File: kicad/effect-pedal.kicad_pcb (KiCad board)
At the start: 2 copper layers, 85 parts, among them J1 NJ3FD-V, J10 USB_C_Receptacle_USB2.0_14P, J11 Conn_ST_STDC14, J12 Barrel_Jack, J2 NJ3FD-V, J3 Conn_01x08, J4 Conn_01x06, J5 Conn_01x06, J6 SOIC Bite Connector, J7 SOIC Bite Connector, J8 SOIC Bite Connector, J9 SOIC Bite Connector, Q1 NMOS, Q2 NMOS, SW1 RotaryEncoder_Switch, SW2 RotaryEncoder_Switch, SW3 RotaryEncoder_Switch, SW4 RotaryEncoder_Switch, SW6 SW_SPDT, SW7 SW_Push, U1 STM32H723ZGTx, U2 PCM5102A, U3 USBLC6-2SC6, U4 TPS62142, Y1 Crystal

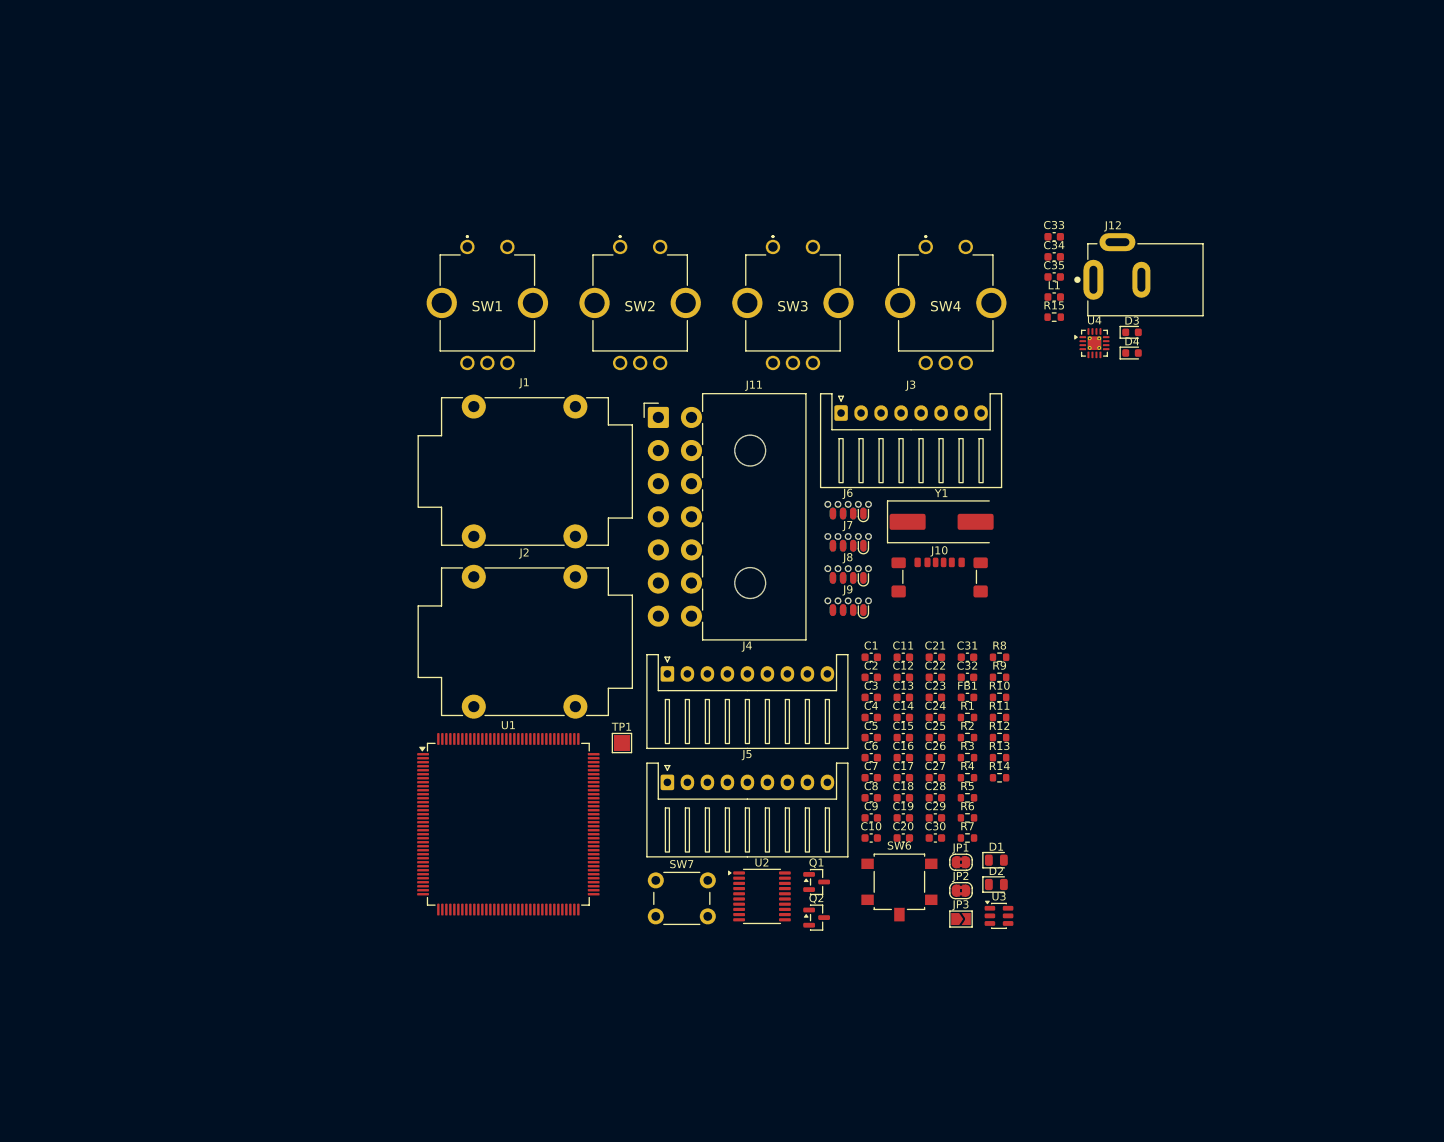
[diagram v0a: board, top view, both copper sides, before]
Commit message: Finish part sourcing and start PCB layout
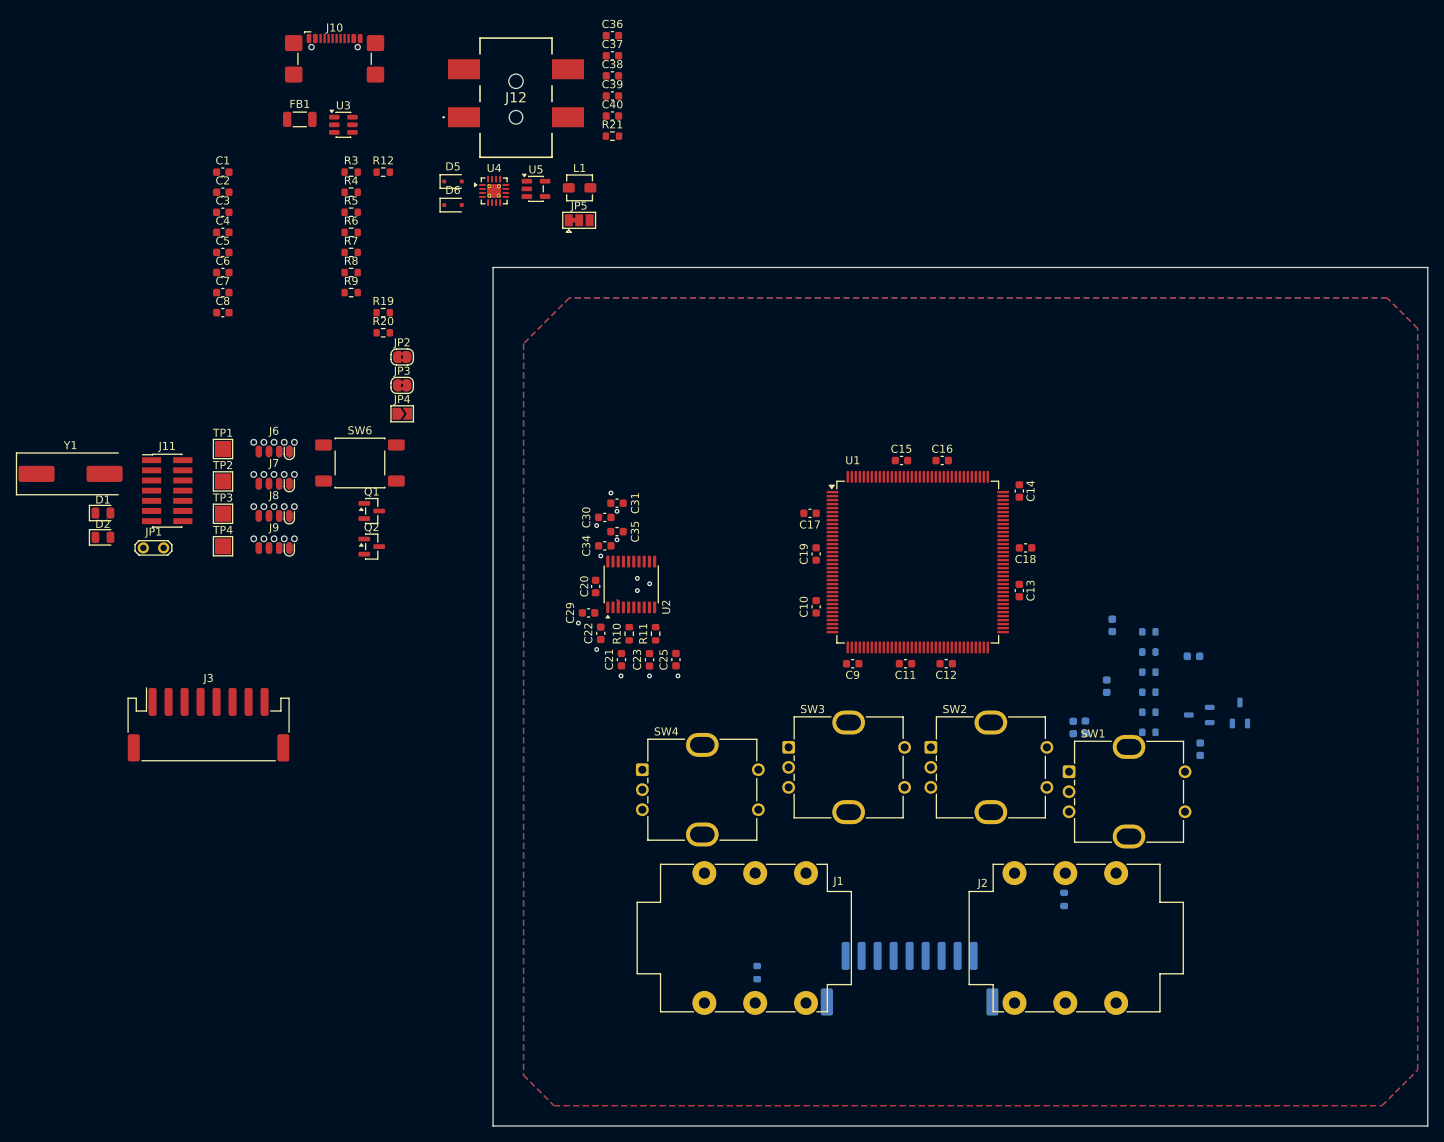
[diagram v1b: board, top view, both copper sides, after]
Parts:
- removed J4: Conn_01x06, Connector_JST:JST_XH_S9B-XH-A_1x09_P2.50mm_Horizontal
- removed SW7: SW_Push, Button_Switch_THT:SW_PUSH_6mm
- added C36: 10u, Capacitor_SMD:C_0603_1608Metric, F.Cu at (105.1, 9.13)
- added C37: 390p, Capacitor_SMD:C_0603_1608Metric, F.Cu at (105.1, 11.6)
- added C38: 22u, Capacitor_SMD:C_0603_1608Metric, F.Cu at (105.1, 14.2)
- added C39: 4.7u, Capacitor_SMD:C_0603_1608Metric, F.Cu at (105.1, 16.7)
- added C40: 1u, Capacitor_SMD:C_0603_1608Metric, F.Cu at (105.1, 19.2)
- added D5: D_Schottky, Diode_SMD:D_SOD-323F, F.Cu at (85.2, 27.4)
- added D6: D_Schottky, Diode_SMD:D_SOD-323F, F.Cu at (85.2, 30.3)
- added JP4: SolderJumper_2_Open, Jumper:SolderJumper-2_P1.3mm_Open_TrianglePad1.0x1.5mm, F.Cu at (78.8, 56.4)
- added JP5: SolderJumper_3_Bridged12, Jumper:SolderJumper-3_P1.3mm_Bridged12_Pad1.0x1.5mm, F.Cu at (100.9, 32.2)
- added R16: 100k, Resistor_SMD:R_0603_1608Metric, B.Cu at (172.1, 91.2)
- added R17: 100, Resistor_SMD:R_0603_1608Metric, B.Cu at (172.1, 93.7)
- added R18: 100, Resistor_SMD:R_0603_1608Metric, B.Cu at (172.1, 96.2)
- added R19: 5.1k, Resistor_SMD:R_0603_1608Metric, F.Cu at (76.4, 43.8)
- added R20: 5.1k, Resistor_SMD:R_0603_1608Metric, F.Cu at (76.4, 46.3)
- added R21: 100k, Resistor_SMD:R_0603_1608Metric, F.Cu at (105.1, 21.7)
- added TP2: TestPoint, TestPoint:TestPoint_Pad_2.0x2.0mm, F.Cu at (56.4, 64.8)
- added TP3: TestPoint, TestPoint:TestPoint_Pad_2.0x2.0mm, F.Cu at (56.4, 68.9)
- added TP4: TestPoint, TestPoint:TestPoint_Pad_2.0x2.0mm, F.Cu at (56.4, 72.9)
- added U5: LP5907MFX-3.0, Package_TO_SOT_SMD:SOT-23-5, F.Cu at (95.5, 28.3)
- C10, C11, C12, C13, C14, C15, C16, C17, C18, C7, C9: value 100n -> 0.1u
- C19: value 10u -> 0.1u
- C20: value 0.1u -> 2.2u
- C23: value 2.2u -> 2.2n
- C24: value 10u -> 0.1u; moved to B.Cu
- C26: value 10n -> 10u; moved to B.Cu
- C27: value 2.2n -> 10u; moved to B.Cu
- C28, R15: moved to B.Cu
- C30: value 15u -> 10u
- C31: value .1u -> 10u
- C32: value .1u -> 10n; moved to B.Cu
- C33: value 10u -> 10n; moved to B.Cu
- C34: value 390p -> 0.1u
- C35: value 22u -> 0.1u
- C8: value 100n -> 1u
- D3, D4: value D -> D_Schottky_Dual_Series_ACK_Split; footprint Diode_SMD:D_0603_1608Metric -> Package_TO_SOT_SMD:TSOT-23; moved to B.Cu
- FB1: footprint Inductor_SMD:L_0603_1608Metric -> Inductor_SMD:L_1206_3216Metric
- J1, J2: value NJ3FD-V -> NJ6FD-H; footprint Connector_Audio:Jack_6.35mm_Neutrik_NMJ4HCD2_Horizontal -> Connector_Audio:Jack_6.35mm_Neutrik_NMJ6HCD3_Horizontal
- J10: footprint Connector_USB:USB_C_Receptacle_GCT_USB4135-GF-A_6P_TopMnt_Horizontal -> Connector_USB:USB_C_Receptacle_GCT_USB4110
- J11: footprint Connector_TE-Connectivity:TE_MATE-N-LOK_1-770973-x_2x07_P4.14mm_Horizontal -> Connector_PinHeader_1.27mm:PinHeader_2x07_P1.27mm_Vertical_SMD
- J12: footprint SameSky:CUI_PJ-002A -> SameSky:PJ002AHSMTTR
- J3: footprint Connector_JST:JST_XH_S8B-XH-A_1x08_P2.50mm_Horizontal -> Connector_JST:JST_PH_S8B-PH-SM4-TB_1x08-1MP_P2.00mm_Horizontal
- J5: value Conn_01x06 -> Conn_01x09; footprint Connector_JST:JST_XH_S9B-XH-A_1x09_P2.50mm_Horizontal -> Connector_JST:JST_PH_S9B-PH-SM4-TB_1x09-1MP_P2.00mm_Horizontal; moved to B.Cu
- JP1: value SolderJumper_2_Bridged -> Jumper_2_Open; footprint Jumper:SolderJumper-2_P1.3mm_Bridged2Bar_RoundedPad1.0x1.5mm -> TestPoint:TestPoint_2Pads_Pitch2.54mm_Drill0.8mm
- JP3: value SolderJumper_2_Open -> SolderJumper_2_Bridged; footprint Jumper:SolderJumper-2_P1.3mm_Open_TrianglePad1.0x1.5mm -> Jumper:SolderJumper-2_P1.3mm_Bridged2Bar_RoundedPad1.0x1.5mm
- L1: footprint Inductor_SMD:L_0603_1608Metric -> Inductor_SMD:L_Vishay_IHLP-1212
- R1: value 100k -> 1M; moved to B.Cu
- R11: value 3.3k -> 470
- R12: value 3.3k -> 100k
- R13, R14: value 5.1k -> 100k; moved to B.Cu
- R2: value 3.3k -> 1M; moved to B.Cu
- R3, R6: value 10k -> 100k
- R4: value 100k -> 3.3k
- R5: value 3.3k -> 10k
- R7: value 10k -> 3.3k
- R8: value 100k -> 10k
- R9: value 470 -> 10k
- SW1, SW2, SW3, SW4: footprint Bournes:PEC11L4115FS0020 -> Bournes:RotaryEncoder_Bourns_Vertical_PEC12R-3x17F-Sxxxx
- SW6: value SW_SPDT -> SW_Push; footprint Button_Switch_SMD:SW_SPST_B3S-1100 -> Button_Switch_SMD:SW_Push_1P1T_NO_E-Switch_TL3301NxxxxxG
- moved U3 128.4 mm to (71.5, 20.3)
- moved D1 119.8 mm to (41.4, 68.8)
- moved D2 119.8 mm to (41.4, 71.8)
- moved FB1 110.4 mm to (66.0, 19.6)
- moved JP1 109.5 mm to (46.5, 73.2)
- moved Y1 109.0 mm to (37.4, 63.9)
- moved R3 106.3 mm to (72.4, 26.2)
- moved R4 106.3 mm to (72.4, 28.7)
- moved R5 106.3 mm to (72.4, 31.2)
- moved R6 106.3 mm to (72.4, 33.7)
- moved R7 106.3 mm to (72.4, 36.2)
- moved R12 104.6 mm to (76.4, 26.2)
- moved C1 101.2 mm to (56.4, 26.2)
- moved C2 101.2 mm to (56.4, 28.7)
- moved C3 101.2 mm to (56.4, 31.2)
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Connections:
- C20 pad 1: VCC -> Net-(U2-CAPM)
- C20 pad 2: GND -> Net-(U2-CAPP)
- C22 pad 1: VCC -> VDDA
- C23 pad 1: Net-(U2-CAPM) -> GND
- C23 pad 2: Net-(U2-CAPP) -> /AUD_WET_L
- C24 pad 1: VCC -> VDDA
- C25 pad 2: /AUD_WET_L -> /AUD_WET_R
- C26 pad 1: GND -> VDDA
- C26 pad 2: Net-(C26-Pad2) -> GND
- C27 pad 1: GND -> /AUD_IN_L
- C27 pad 2: /AUD_WET_R -> Net-(C27-Pad2)
- C28 pad 1: Net-(U2-LDOO) -> /AUD_IN_R
- C28 pad 2: GND -> Net-(C28-Pad2)
- C30 pad 1: Net-(C26-Pad2) -> VCC
- C30 pad 2: /AUD_IN_GND -> GND
- C32 pad 2: VDDA -> /AUD_IN_L_BIAS
- C33 pad 1: /Power/VIN -> GND
- C33 pad 2: GND -> /AUD_IN_R_BIAS
- C34 pad 1: Net-(U4-SS/TR) -> VCC
- C35 pad 1: VCC -> GND
- C35 pad 2: GND -> Net-(U2-LDOO)
- C8 pad 1: VCC -> GND
- C8 pad 2: GND -> /VREF+
- D3 pad 1: /Power/VIN -> GND
- D3 pad 2: USB_VBUS -> /VREF+
- D4 pad 1: /Power/VIN -> GND
- D4 pad 2: Net-(D4-A) -> /VREF+
- J1 pad S: /AUD_IN_GND -> GND
- J1 pad SN: (no net) -> /AUD_N
- J1 pad TN: (no net) -> /AUD_N
- J10 pad S1: /SHIELD -> GNDPWR
- J12 pad 2: Net-(D4-A) -> Net-(D6-A)
- J12 pad 3: (no net) -> GNDPWR
- J2 pad SN: (no net) -> /AUD_N
- J2 pad TN: (no net) -> /AUD_N
- J3 pad 1: VCC -> /DISPLAY_BL
- J3 pad 2: GND -> /DISPLAY_RST
- J3 pad 3: /DISPLAY_DATA -> /DISPLAY_DC
- J3 pad 4: /DISPLAY_SCK -> /DISPLAY_CS
- J3 pad 5: /DISPLAY_CS -> /DISPLAY_SCK
- J3 pad 6: /DISPLAY_DC -> /DISPLAY_DATA
- J3 pad 7: /DISPLAY_RST -> GND
- J3 pad 8: /DISPLAY_BL -> VCC
- J5 pad 3: /AUD_IN_GND -> GND
- J6 pad 1: /AUD_IN_R_AMP -> /AUD_IN_R_BIAS
- J6 pad 3: /AUD_IN_L_AMP -> /AUD_IN_L_BIAS
- J6 pad 7: /AUD_IN_GND -> /AUD_IN_R_AMP
- JP1 pad 1: /DEBUG_RST -> VCC
- JP1 pad 2: /RESET -> /BOOT
- JP2 pad 1: VCC -> /DEBUG_RST
- JP2 pad 2: Net-(JP2-B) -> /RESET
- JP3 pad 2: /VREF+ -> Net-(JP3-B)
- R1 pad 1: /LED_1 -> /AUD_N
- R10 pad 1: Net-(U2-OUTR) -> /AUD_WET_L
- R10 pad 2: /AUD_WET_R -> Net-(U2-OUTL)
- R11 pad 1: /VREF+ -> /AUD_WET_R
- R11 pad 2: Net-(C26-Pad2) -> Net-(U2-OUTR)
- R12 pad 1: Net-(C26-Pad2) -> GNDPWR
- R13 pad 1: /CC2 -> /VREF+
- R13 pad 2: GND -> Net-(C27-Pad2)
- R14 pad 1: /CC1 -> Net-(C27-Pad2)
- R15 pad 1: VCC -> /VREF+
- R15 pad 2: Net-(U4-PG) -> Net-(C28-Pad2)
- R2 pad 1: VCC -> /AUD_N
- R2 pad 2: Net-(Q1-D) -> GND
- R3 pad 1: /BOOT -> /LED_1
- R3 pad 2: Net-(SW6-B) -> GND
- R4 pad 1: /LED_2 -> VCC
- R4 pad 2: GND -> Net-(Q1-D)
- R5 pad 1: VCC -> /BOOT
- R5 pad 2: Net-(Q2-D) -> GND
- R6 pad 1: VCC -> /LED_2
- R6 pad 2: /RESET -> GND
- R7 pad 1: /UNUSED -> VCC
- R7 pad 2: GND -> Net-(Q2-D)
- R8 pad 1: GND -> VCC
- R8 pad 2: /SHIELD -> /RESET
- R9 pad 1: /AUD_WET_L -> /UNUSED
- R9 pad 2: Net-(U2-OUTL) -> GND
- SW6 pad 2: Net-(SW6-B) -> /RESET
- TP1 pad 1: Net-(U1-VBAT) -> VCC
- U1 pad 46: /AUD_IN_R -> /AUD_IN_R_BIAS
- U1 pad 6: Net-(U1-VBAT) -> VCC
- U1 pad 60: /AUD_IN_L -> /AUD_IN_L_BIAS
- U1 pad 95: Net-(JP2-B) -> Net-(JP3-B)
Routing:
- net GND: track 0.00 -> 0.93 mm, vias 0 -> 11
- net VCC: vias 0 -> 2
- added copper zone on B.Cu, net GND
- added copper zone on F.Cu, net GND
- added copper zone on In1.Cu, net GND
- added copper zone on In2.Cu, net VCC
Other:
- board outline added: 116.8 x 107.3 mm
- copper layers 2 -> 4

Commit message: Finish schematic
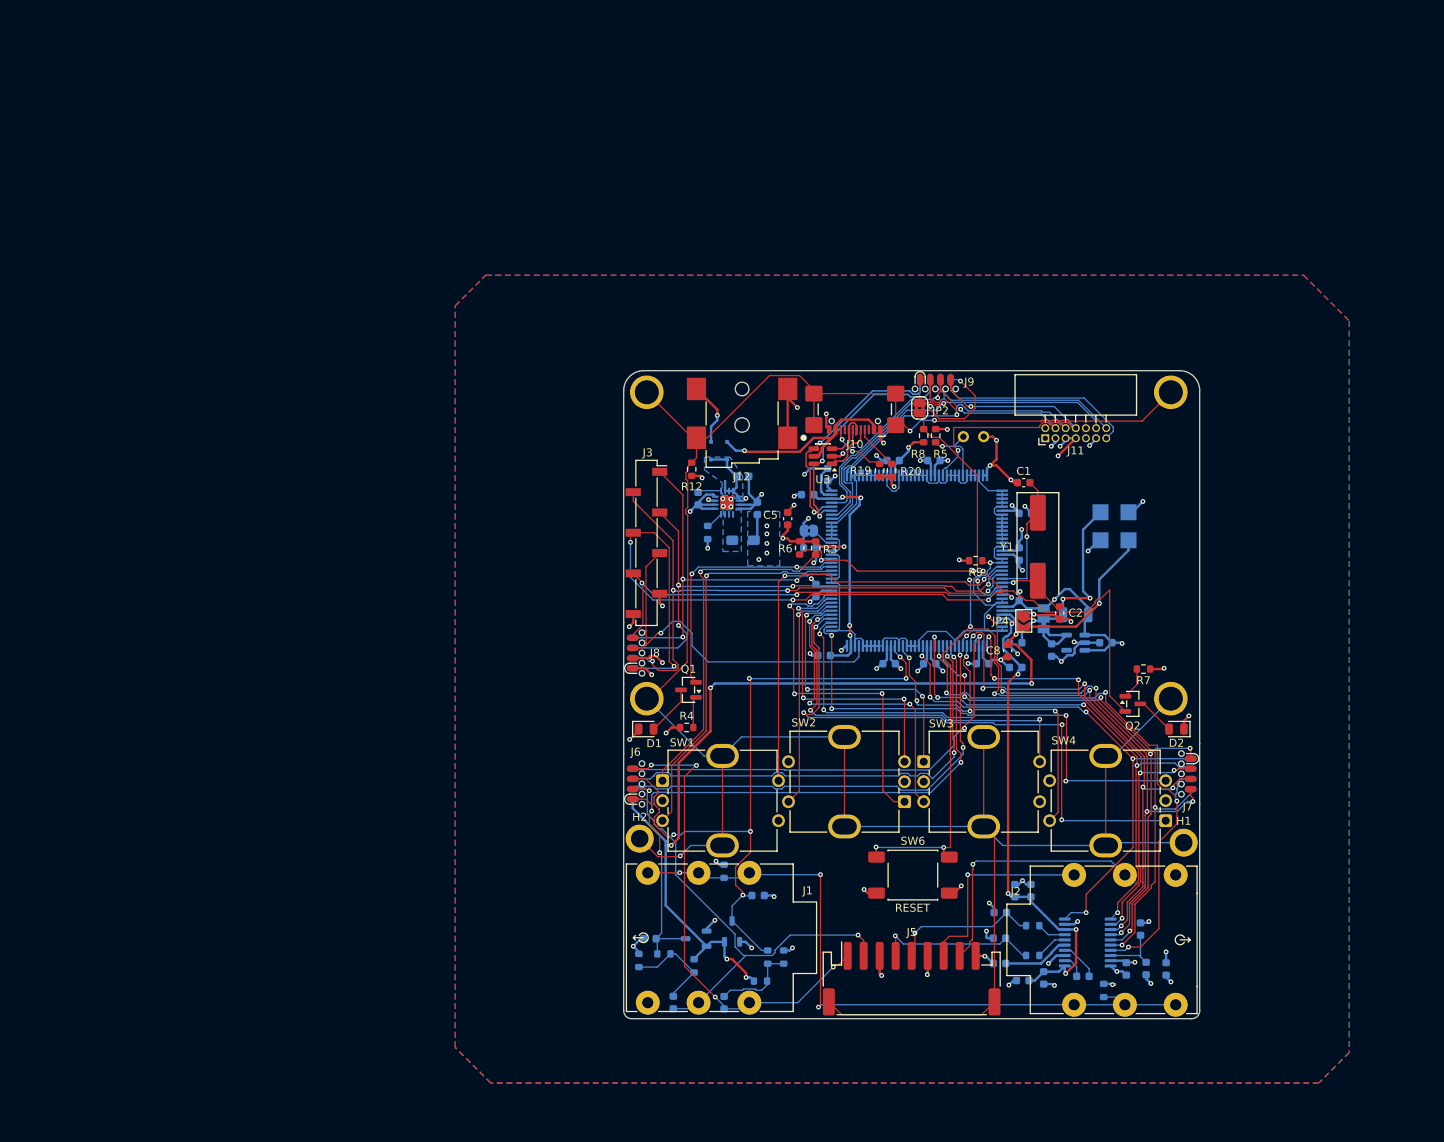
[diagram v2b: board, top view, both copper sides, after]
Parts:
- added H1: MountingHole_Pad, MountingHole:MountingHole_2.2mm_M2_ISO7380_Pad, F.Cu at (176.5, 110.0)
- added H2: MountingHole_Pad, MountingHole:MountingHole_2.2mm_M2_ISO7380_Pad, F.Cu at (108.5, 109.5)
- C10, C11, C12, C13, C14, C15, C16, C17, C18, C19, C20, C21, C22, C23, C25, C29, C3, C30, C31, C34, C35, C36, C37, C38, C39, C4, C40, C6, C7, C9, D5, D6, FB1, JP1, JP3, JP5, L1, R10, R11, R21, TP1, TP2, TP3, TP4, U1, U2, U4, U5: moved to B.Cu
- J1, J2: value NJ6FD-H -> NMJ6HCD3; footprint Connector_Audio:Jack_6.35mm_Neutrik_NMJ6HCD3_Horizontal -> Neutrik:Jack_6.35mm_Neutrik_NMJ6HCD3_Horizontal
- J10: footprint Connector_USB:USB_C_Receptacle_GCT_USB4110 -> Custom:USB_C_Receptacle_GCT_USB4110
- J11: footprint Connector_PinHeader_1.27mm:PinHeader_2x07_P1.27mm_Vertical_SMD -> Custom:STDC14_Connector
- J12: footprint SameSky:PJ002AHSMTTR -> Custom:CUI_PJ-002AH-SMT-TR
- J3: footprint Connector_JST:JST_PH_S8B-PH-SM4-TB_1x08-1MP_P2.00mm_Horizontal -> Waveshare:Waveshare_2.4in_LCD
- J5: footprint Connector_JST:JST_PH_S9B-PH-SM4-TB_1x09-1MP_P2.00mm_Horizontal -> Custom:JST_PH_S9B-PH-SM4-TB_1x09-1MP_P2.00mm_Horizontal; moved to F.Cu
- moved D2 136.3 mm to (175.6, 95.8), turned to 180 degrees
- moved Y1 121.3 mm to (158.3, 73.0), turned to -90 degrees
- moved J7 120.7 mm to (178.1, 101.4), turned to 90 degrees
- moved C2 117.1 mm to (161.0, 81.3), turned to -90 degrees
- moved FB1 115.1 mm to (163.0, 81.5), turned to 180 degrees
- moved TP1 113.5 mm to (169.6, 68.7), turned to 180 degrees
- moved TP3 113.2 mm to (169.6, 72.2), turned to 180 degrees
- moved R7 111.9 mm to (171.5, 88.3), turned to 180 degrees
- moved C6 110.7 mm to (155.5, 88.1), turned to 180 degrees
- moved J11 110.0 mm to (159.2, 59.5), turned to 90 degrees
- moved TP2 109.8 mm to (166.1, 68.7), turned to 180 degrees
- moved TP4 109.7 mm to (166.1, 72.2), turned to 180 degrees
- moved C7 108.3 mm to (155.5, 85.0), turned to 180 degrees
- moved C1 107.4 mm to (156.5, 65.0)
- moved C8 106.8 mm to (154.5, 86.0), turned to 90 degrees
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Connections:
- net Net-(D6-A) renamed /Power/VIN_JACK
- net Net-(JP5-A) renamed /Power/PWR_LDO_OUT
- net Net-(L1-Pad1) renamed /Power/PWR_SW
- net Net-(U4-PG) renamed /Power/PG
- net Net-(U4-SS/TR) renamed /Power/SS
- JP4 pad 1: VCC -> VDDA
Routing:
- net GNDPWR: track 0.00 -> 301.2 mm, vias 0 -> 3
- net GND: track 0.93 -> 173.2 mm, vias 11 -> 64
- net /VREF+: track 0.00 -> 130.2 mm, vias 0 -> 7
- net /UNUSED: track 0.00 -> 126.0 mm, vias 0 -> 1
- net VCC: track 0.00 -> 97.5 mm, vias 2 -> 34
- net VDDA: track 0.00 -> 87.4 mm, vias 0 -> 8
- net /AUD_IN_L_BIAS: track 0.00 -> 85.8 mm, vias 0 -> 6
- net /AUD_IN_R_BIAS: track 0.00 -> 83.4 mm, vias 0 -> 4
- net /AUD_N: track 0.00 -> 83.2 mm, vias 0 -> 3
- net /DISPLAY_CS: track 0.00 -> 78.9 mm, vias 0 -> 4
- net /RESET: track 0.00 -> 77.9 mm, vias 0 -> 5
- net /DISPLAY_RST: track 0.00 -> 74.2 mm, vias 0 -> 4
- net /EDAC_XSMT: track 0.00 -> 73.9 mm, vias 0 -> 5
- net /ENC4_L: track 0.00 -> 73.1 mm, vias 0 -> 4
- net /DISPLAY_BL: track 0.00 -> 70.1 mm, vias 0 -> 4
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- added copper zone on B.Cu, net /Power/PWR_SW
- added copper zone on B.Cu, net /Power/VIN
- added copper zone on B.Cu, net VCC
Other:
- board size 116.8 x 107.3 mm -> 72 x 81 mm
- board text added: "Digital Effect Pedal v1 Edith Boles Ethan Ferguson Muhammad-Abdullah Abdelqader Nick Nikander Shaelin Olton"
- board text added: "GND"
- board text added: "RESET"
- board text added: "VCC"
- board text added: "VDDA"
- board text added: "VREF+"

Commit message: Setup for production
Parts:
- U4: footprint Package_DFN_QFN:VQFN-16-1EP_3x3mm_P0.5mm_EP1.68x1.68mm_ThermalVias -> Custom:VQFN-16-1EP_3x3mm_P0.5mm_EP1.68x1.68mm_ThermalVias
- moved TP1 5.20 mm to (169.6, 63.5)
- moved TP2 5.20 mm to (166.1, 63.5)
- moved TP3 5.20 mm to (169.6, 67.0)
- moved TP4 5.20 mm to (166.1, 67.0)
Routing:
- net VDDA: track 87.4 -> 93.3 mm
- net /VREF+: track 130.2 -> 135.3 mm
- net /LED_1: track 35.0 -> 38.3 mm
- net /ENC1_B: track 31.8 -> 34.7 mm
- net GNDPWR: track 301.2 -> 300.2 mm
- net /ENC4_R: track 63.7 -> 63.0 mm
- net /ENC4_B: track 55.1 -> 54.5 mm
- net /ENC3_L: track 36.0 -> 35.3 mm
- net /ENC2_B: track 28.8 -> 28.1 mm
- net /ENC2_R: track 36.6 -> 36.0 mm
- net /AUD_WET_R: track 18.7 -> 18.1 mm
- net VCC: track 97.5 -> 97.0 mm
- net GND: track 173.2 -> 173.5 mm, vias 64 -> 75

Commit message: Update FFT to read from dac
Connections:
- Q1 pad 2: /LED_1 -> Net-(D1-A)
- Q1 pad 3: Net-(D1-A) -> /LED_1
- Q2 pad 2: /LED_2 -> Net-(D2-A)
- Q2 pad 3: Net-(D2-A) -> /LED_2
